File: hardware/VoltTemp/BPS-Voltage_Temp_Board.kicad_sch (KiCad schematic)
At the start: 10 parts, among them J2 PeripheralCAN, J3 PeripheralCAN, J5 Logic_Analyzer, U5 PeripheralSOM

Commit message: schematic mostly done
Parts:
- removed J3: PeripheralCAN, UTSVT_Connectors:Molex_Nano-Fit_105309-xx04_1x04_P2.50mm_Vertical, symbol utsvt_connectors:PeripheralCANConnector
- removed U5: PeripheralSOM, UTSVT_Special:PeripheralSOM, symbol utsvt-misc:PeripheralSOM
- added J10: 53307-2471, UTSVT_Connectors:533072471, symbol utsvt_connectors:PeripheralSOMConnector
- added J12, J13: Conn_01x04, VoltTemp:1053132104, symbol Connector_Generic:Conn_01x04
- added R29: 0Ω, Resistor_SMD:R_0603_1608Metric_Pad0.98x0.95mm_HandSolder, symbol Device:R
- J2: now not fitted; now left out of the parts list
- J5: footprint CONN_SFH11-xxxC-D05-ST-XX_SUL -> UTSVT_Connectors:CONN_SFH11-xxxC-D05-ST-XX_SUL
- LOGO1: footprint UTSVT_Logos:Hallock_Image_Tiny -> UTSVT_Logos:Hallock_Image_Small
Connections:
- net +24V: now also J10.24 (+24V_In), J12.1 (Pin_1), J13.1 (Pin_1); no longer J2.1 (24V)
- net +3.3V: now also J10.2 (+3.3v), R29.2
- net GND: now also J10.1 (GND), J10.3 (GND), J10.5 (GND), J12.4 (Pin_4), J13.4 (Pin_4); no longer J2.2 (GND)
- net GNDA: now also J10.10 (GNDA)
- net I-CAN_H: now also J10.22 (CAN_H), J12.2 (Pin_2), J13.2 (Pin_2); no longer J2.3 (CAN_H)
- net I-CAN_L: now also J10.20 (CAN_L), J12.3 (Pin_3), J13.3 (Pin_3); no longer J2.4 (CAN_L)
- net I2C_SCL: now also J10.6 (I2C1_SCL)
- net I2C_SDA: now also J10.4 (I2C1_SDA)
- net bmsAlert: now also J10.12 (SPI2_NSS)
- net bmsEn: now also J10.19 (SPI1_NSS)
- net LedDin: now reaches J5.5 (CH4)
- net LedDin: now also J10.18 (SPI2_SCK)
- net PB3: now reaches J5.6 (CH5)
- net PB3: now also J10.23 (SPI1_SCK)
- new net Temperature0: J10.9 (ADC1_IN7)
- new net Temperature1: J10.11 (ADC1_IN9)
- new net Temperature2: J10.13 (ADC1_IN10)
- new net Temperature3: J10.15 (ADC1_IN11)
- new net VDDA: J10.8 (VDDA), R29.1
- no-connect marks 14 -> 7
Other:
- added sheet FaultIndicators (FaultIndicators.kicad_sch)
- note added: "PeripheralCAN Connector For pin number reference"
- note added: "Schematic Todo: - Proper CubeMX pinout [X] - Add extra GPIO pins to logic analyzer [] - Assign footprints and P/N [X] - Assign LSC P/N [] - Temperature op amp values - Add debouncing to bms boot button [] - Fix i2c bus[] - LTSpice screenshots for thermistor [] - Derate PTC fuses [] - Add EL3H7 to dl [X] - Make sure optos are fine when regout is 2.5V [X] - Molex Connector pn [X] - Fix all the data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"

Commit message: layout
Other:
- note added: "Schematic Todo: - Proper CubeMX pinout [X] - Add extra GPIO pins to logic analyzer [] - Assign footprints and P/N [X] - Assign LSC P/N [] - Temperature op amp values [] - Add debouncing to bms boot button [] - Fix i2c bus[] - LTSpice screenshots for thermistor [] - Derate PTC fuses [] - Add EL3H7 to dl [X] - Make sure optos are fine when regout is 2.5V [X] - Molex Connector pn [X] - Fix all the d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"
- note removed: "Schematic Todo: - Proper CubeMX pinout [X] - Add extra GPIO pins to logic analyzer [] - Assign footprints and P/N [X] - Assign LSC P/N [] - Temperature op amp values - Add debouncing to bms boot button [] - Fix i2c bus[] - LTSpice screenshots for thermistor [] - Derate PTC fuses [] - Add EL3H7 to dl [X] - Make sure optos are fine when regout is 2.5V [X] - Molex Connector pn [X] - Fix all the data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"
- moved on the sheet: J2
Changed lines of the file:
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@@
 		(comment 4 "Board for measuring voltage and temperature of the battery modules.")
 	)
+	(bus_alias "I2C"
+		(members "I2C_SDA" "I2C_SCL")
+	)
 	(rectangle
 		(start 157.48 67.945)
@@
 		)
 	)
-	(text "Schematic Todo:\n- Proper CubeMX pinout [X]\n- Add extra GPIO pins to logic analyzer []\n- Assign footprints and P/N [X]\n- Assign LSC P/N []\n- Temperature op amp values\n- Add debouncing to bms boot button []\n- Fix i2c bus[]\n- LTSpice screenshots for thermistor []\n- Derate PTC fuses []\n- Add EL3H7 to dl [X]\n- Make sure optos are fine when regout is 2.5V [X]\n- Molex Connector pn [X]\n- Fix all the datasheet as embed symbols [X]\n- Add bypass caps to i2c isolator [X]\n- Change CAN and power connector [X]\n- Fix PB16 (overlapping with PP IMON []"
+	(text "Schematic Todo:\n- Proper CubeMX pinout [X]\n- Add extra GPIO pins to logic analyzer []\n- Assign footprints and P/N [X]\n- Assign LSC P/N []\n- Temperature op amp values []\n- Add debouncing to bms boot button []\n- Fix i2c bus[]\n- LTSpice screenshots for thermistor []\n- Derate PTC fuses []\n- Add EL3H7 to dl [X]\n- Make sure optos are fine when regout is 2.5V [X]\n- Molex Connector pn [X]\n- Fix all the datasheet as embed symbols [X]\n- Add bypass caps to i2c isolator [X]\n- Change CAN and power connector [X]\n- Fix PB16 (overlapping with PP IMON []"
 		(exclude_from_sim no)
 		(at 94.488 167.894 0)
@@
 	(text "PeripheralCAN Connector\nFor pin number reference"
 		(exclude_from_sim no)
-		(at 164.592 43.18 0)
+		(at 164.338 41.656 0)
 		(effects
 			(font
@@
 	(wire
 		(pts
-			(xy 222.25 115.57) (xy 222.25 116.84)
-		)
-		(stroke
-			(width 0)
-			(type default)
-		)
-	)
-	(wire
-		(pts
 			(xy 190.5 35.56) (xy 191.77 35.56)
 		)
@@
 			"rq6p7tKZVhPk8qVwiDi6OtuUFEs+tRON4MrtlEqKyxzhbmH55dR3qR2pF1NjnqVX/+s0jXbd2u79"
 			"LanTqR8XULry74dSg9ntR/9O19Jhb9O61z7+uMsTT6ZeSZ05mDq3cCW1vyg4soEQ6R/yLmIm18Tb"
-			"GxuVOKNKo7+z3Mi4qZE6DZJBIg=="
+			"GxuVOKNKo7+z3Mi4qZE6DZJBIgAkAADlGAAADwAAAOUYAAAPAAAA/////wAkAAD0GAAADwAAAPQY"
+			"AAAPAAAA/////wAkAAADGQAADwAAAAMZAAAPAAAA/////wAkAAASGQAADgAAABIZAAAOAAAA////"
+			"/wAkAAAgGQAABAAAACAZAAAEAAAA/////wAkAAAkGQAACQAAACQZAAAJAAAA/////wAkAAAtGQAA"
+			"BAAAAC0ZAAAEAAAA/////wAkAAAxGQAABAAAADEZAAAEAAAA/////wAkAAA1GQAABgAAADUZAAAG"
+			"AAAA/////wAkAAA7GQAABAAAADsZAAAEAAAA/////wAkAAA/GQAABAAAAD8ZAAAEAAAA/////wAk"
+			"AABDGQAACAAAAEMZAAAIAAAA/////wAkAABLGQAACAAAAEsZAAAIAAAA/////wAkAABTGQAABgAA"
+			"AFMZAAAGAAAA/////wAkAABZGQAABgAAAFkZAAAGAAAA/////wAkAABfGQAABwAAAF8ZAAAHAAAA"
+			"/////wAkAABmGQAABwAAAGYZAAAHAAAA/////wAkAABtGQAACAAAAG0ZAAAIAAAA/////wAkAAB1"
+			"GQAACAAAAHUZAAAIAAAA/////wAkAAB9GQAADAAAAH0ZAAAMAAAA/////wAkAACJGQAAEgAAAIkZ"
+			"AAASAAAA/////wAkAACbGQAAEAAAAJsZAAAQAAAA/////wAkAACrGQAAEQAAAKsZAAARAAAA////"
+			"/wAkAAC8GQAAEAAAALwZAAAQAAAA/////wAkAADMGQAAEQAAAMwZAAARAAAA/////wAkAADdGQAA"
+			"FAAAAN0ZAAAUAAAA/////wAkAADxGQAAEwAAAPEZAAATAAAA/////wAkAAAEGgAAEwAAAAQaAAAT"
+			"AAAA/////wAkAAAXGgAAEwAAABcaAAATAAAA/////wAkAAAqGgAAEwAAACoaAAATAAAA/////wgk"
+			"AAA9GgAAFAAAAD0aAAAUAAAA/////wAkAABRGgAAEwAAAFEaAAATAAAA/////wgkAABkGgAAEwAA"
+			"AGQaAAATAAAA/////wAkAAB3GgAADQAAAHcaAAANAAAA/////wAkAACEGgAAEQAAAIQaAAARAAAA"
+			"/////wgkAACVGgAAFAAAAJUaAAAUAAAA/////wAkAACpGgAADwAAAKkaAAAPAAAA/////wAkAAC4"
+			"GgAAFAAAALgaAAAUAAAA/////wAkAADMGgAAEgAAAMwaAAASAAAA/////wAkAADeGgAAEAAAAN4a"
+			"AAAQAAAA/////wAkAADuGgAAFAAAAO4aAAAUAAAA/////wAkAAACGwAAFQAAAAIbAAAVAAAA////"
+			"/wAkAAAXGwAAFAAAABcbAAAUAA=="
 		)
 	)
@@
 	(symbol
 		(lib_id "power:+3.3V")
-		(at 222.25 115.57 0)
+		(at 222.25 116.84 0)
 		(unit 1)
 		(exclude_from_sim no)
@@
 		(fields_autoplaced yes)
 		(property "Reference" "#PWR080"
-			(at 222.25 119.38 0)
+			(at 222.25 120.65 0)
 			(effects
 				(font
@@
 		)
 		(property "Value" "+3.3V"
-			(at 222.25 110.49 0)
+			(at 222.25 111.76 0)
 			(effects
 				(font
@@
 		)
 		(property "Footprint" ""
-			(at 222.25 115.57 0)
+			(at 222.25 116.84 0)
 			(effects
 				(font
@@
 		)
 		(property "Datasheet" ""
-			(at 222.25 115.57 0)
+			(at 222.25 116.84 0)
 			(effects
 				(font
@@
 		)
 		(property "Description" "Power symbol creates a global label with name \"+3.3V\""
-			(at 222.25 115.57 0)
+			(at 222.25 116.84 0)
 			(effects
 				(font
@@
 	(symbol
 		(lib_id "utsvt_connectors:PeripheralCANConnector")
-		(at 160.02 33.02 0)
+		(at 160.02 31.75 0)
 		(unit 1)
 		(exclude_from_sim yes)
@@
 		(fields_autoplaced yes)
 		(property "Reference" "J2"
-			(at 160.655 22.86 0)
+			(at 160.655 21.59 0)
 			(effects
 				(font
@@
 		)
 		(property "Value" "PeripheralCAN"
-			(at 160.655 25.4 0)
+			(at 160.655 24.13 0)
 			(effects
 				(font
@@
 		)
 		(property "Footprint" "UTSVT_Connectors:Molex_Nano-Fit_105309-xx04_1x04_P2.50mm_Vertical"
-			(at 160.02 41.91 0)
+			(at 160.02 40.64 0)
 			(effects
 				(font
@@
 		)
 		(property "Datasheet" "https://www.mouser.com/ProductDetail/Molex/105309-1204?qs=PqFvFmEiOr6mDAWV2BJKbg%3D%3D&srsltid=AfmBOopk7YsqdMLo2_DAHKaHKt3Hg126ooPXYWv5Q2Pfx6rW7DaYZCT2"
-			(at 165.1 25.4 0)
+			(at 165.1 24.13 0)
 			(effects
 				(font
@@
 		)
 		(property "Description" "Connection to the car's Peripheral CAN bus."
-			(at 160.02 33.02 0)
+			(at 160.02 31.75 0)
 			(effects
 				(font
@@
 		)
 		(property "P/N" "105309-1204 "
-			(at 160.02 33.02 0)
+			(at 160.02 31.75 0)
 			(effects
 				(font

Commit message: layout2 electric boogaloo
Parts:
- added R14, R15: 10kΩ, Resistor_SMD:R_0603_1608Metric_Pad0.98x0.95mm_HandSolder, symbol Device:R
- J10: footprint UTSVT_Connectors:533072471 -> UTSVT_Connectors:PeripheralSOM
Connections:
- net +3.3V: now also R14.2, R15.2
- net I2C_SCL: now also J5.8 (CH7), R15.1; no longer J5.2 (CH1)
- net I2C_SDA: now also J5.7 (CH6), R14.1; no longer J5.1 (CH0)
- no-connect marks 7 -> 12
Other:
- note added: "Schematic Todo: - Proper CubeMX pinout [X] - Add extra GPIO pins to logic analyzer [] - Assign footprints and P/N [X] - Assign LSC P/N [] - Temperature op amp values [] - Fix i2c bus[X] - LTSpice screenshots for thermistor [] - Derate PTC fuses [] - Add EL3H7 to dl [X] - Make sure optos are fine when regout is 2.5V [X] - Molex Connector pn [X] - Fix all the datasheet as embed symbols [X] - Add by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"
- note removed: "Schematic Todo: - Proper CubeMX pinout [X] - Add extra GPIO pins to logic analyzer [] - Assign footprints and P/N [X] - Assign LSC P/N [] - Temperature op amp values [] - Add debouncing to bms boot button [] - Fix i2c bus[] - LTSpice screenshots for thermistor [] - Derate PTC fuses [] - Add EL3H7 to dl [X] - Make sure optos are fine when regout is 2.5V [X] - Molex Connector pn [X] - Fix all the d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"
- moved on the sheet: R29

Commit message: most layout done
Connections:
- net Temperature0: now also J10.7 (OPAMP1_VINP); no longer J10.9 (ADC1_IN7)
- net Temperature1: now also J10.15 (ADC1_IN11); no longer J10.11 (ADC1_IN9)
- net Temperature3: now also J10.11 (ADC1_IN9); no longer J10.15 (ADC1_IN11)
- net Temperature4: now also J10.9 (ADC1_IN7)
- net PB15: now reaches J5.1 (CH0)
- net PB15: now also J10.16 (SPI2_MOSI)
- net PB14: now reaches J5.2 (CH1)
- net PB14: now also J10.14 (SPI2_MISO)
- no-connect marks 12 -> 10
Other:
- sheet VoltageConn ports: added last_cell; removed none
- sheet VoltageSense ports: added last_cell; removed none
- note added: "Schematic Todo: - Proper CubeMX pinout [X] - Add extra GPIO pins to logic analyzer [] - Assign footprints and P/N [X] - Assign LSC P/N [] - Temperature op amp values [X] - Fix i2c bus[X] - LTSpice screenshots for thermistor [X] - Derate PTC fuses [] - Add EL3H7 to dl [X] - Make sure optos are fine when regout is 2.5V [X] - Molex Connector pn [X] - Fix all the datasheet as embed symbols [X] - Add 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"
- note removed: "Schematic Todo: - Proper CubeMX pinout [X] - Add extra GPIO pins to logic analyzer [] - Assign footprints and P/N [X] - Assign LSC P/N [] - Temperature op amp values [] - Fix i2c bus[X] - LTSpice screenshots for thermistor [] - Derate PTC fuses [] - Add EL3H7 to dl [X] - Make sure optos are fine when regout is 2.5V [X] - Molex Connector pn [X] - Fix all the datasheet as embed symbols [X] - Add by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"

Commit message: some ocd stuff
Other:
- note added: "Schematic Todo: - Proper CubeMX pinout [X] - Add extra GPIO pins to logic analyzer [X] - Assign footprints and P/N [X] - Assign LSC P/N [] - Temperature op amp values [X] - Fix i2c bus[X] - LTSpice screenshots for thermistor [X] - Derate PTC fuses [] - Add EL3H7 to dl [X] - Make sure optos are fine when regout is 2.5V [X] - Molex Connector pn [X] - Fix all the datasheet as embed symbols [X] - Add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"
- note removed: "Schematic Todo: - Proper CubeMX pinout [X] - Add extra GPIO pins to logic analyzer [] - Assign footprints and P/N [X] - Assign LSC P/N [] - Temperature op amp values [X] - Fix i2c bus[X] - LTSpice screenshots for thermistor [X] - Derate PTC fuses [] - Add EL3H7 to dl [X] - Make sure optos are fine when regout is 2.5V [X] - Molex Connector pn [X] - Fix all the datasheet as embed symbols [X] - Add 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"
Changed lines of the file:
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@@
 		)
 	)
-	(text "Schematic Todo:\n- Proper CubeMX pinout [X]\n- Add extra GPIO pins to logic analyzer []\n- Assign footprints and P/N [X]\n- Assign LSC P/N []\n- Temperature op amp values [X]\n- Fix i2c bus[X]\n- LTSpice screenshots for thermistor [X]\n- Derate PTC fuses []\n- Add EL3H7 to dl [X]\n- Make sure optos are fine when regout is 2.5V [X]\n- Molex Connector pn [X]\n- Fix all the datasheet as embed symbols [X]\n- Add bypass caps to i2c isolator [X]\n- Change CAN and power connector [X]\n- Fix PB16 (overlapping with PP IMON [X]"
+	(text "Schematic Todo:\n- Proper CubeMX pinout [X]\n- Add extra GPIO pins to logic analyzer [X]\n- Assign footprints and P/N [X]\n- Assign LSC P/N []\n- Temperature op amp values [X]\n- Fix i2c bus[X]\n- LTSpice screenshots for thermistor [X]\n- Derate PTC fuses []\n- Add EL3H7 to dl [X]\n- Make sure optos are fine when regout is 2.5V [X]\n- Molex Connector pn [X]\n- Fix all the datasheet as embed symbols [X]\n- Add bypass caps to i2c isolator [X]\n- Change CAN and power connector [X]\n- Fix PB16 (overlapping with PP IMON [X]"
 		(exclude_from_sim no)
 		(at 94.488 167.894 0)

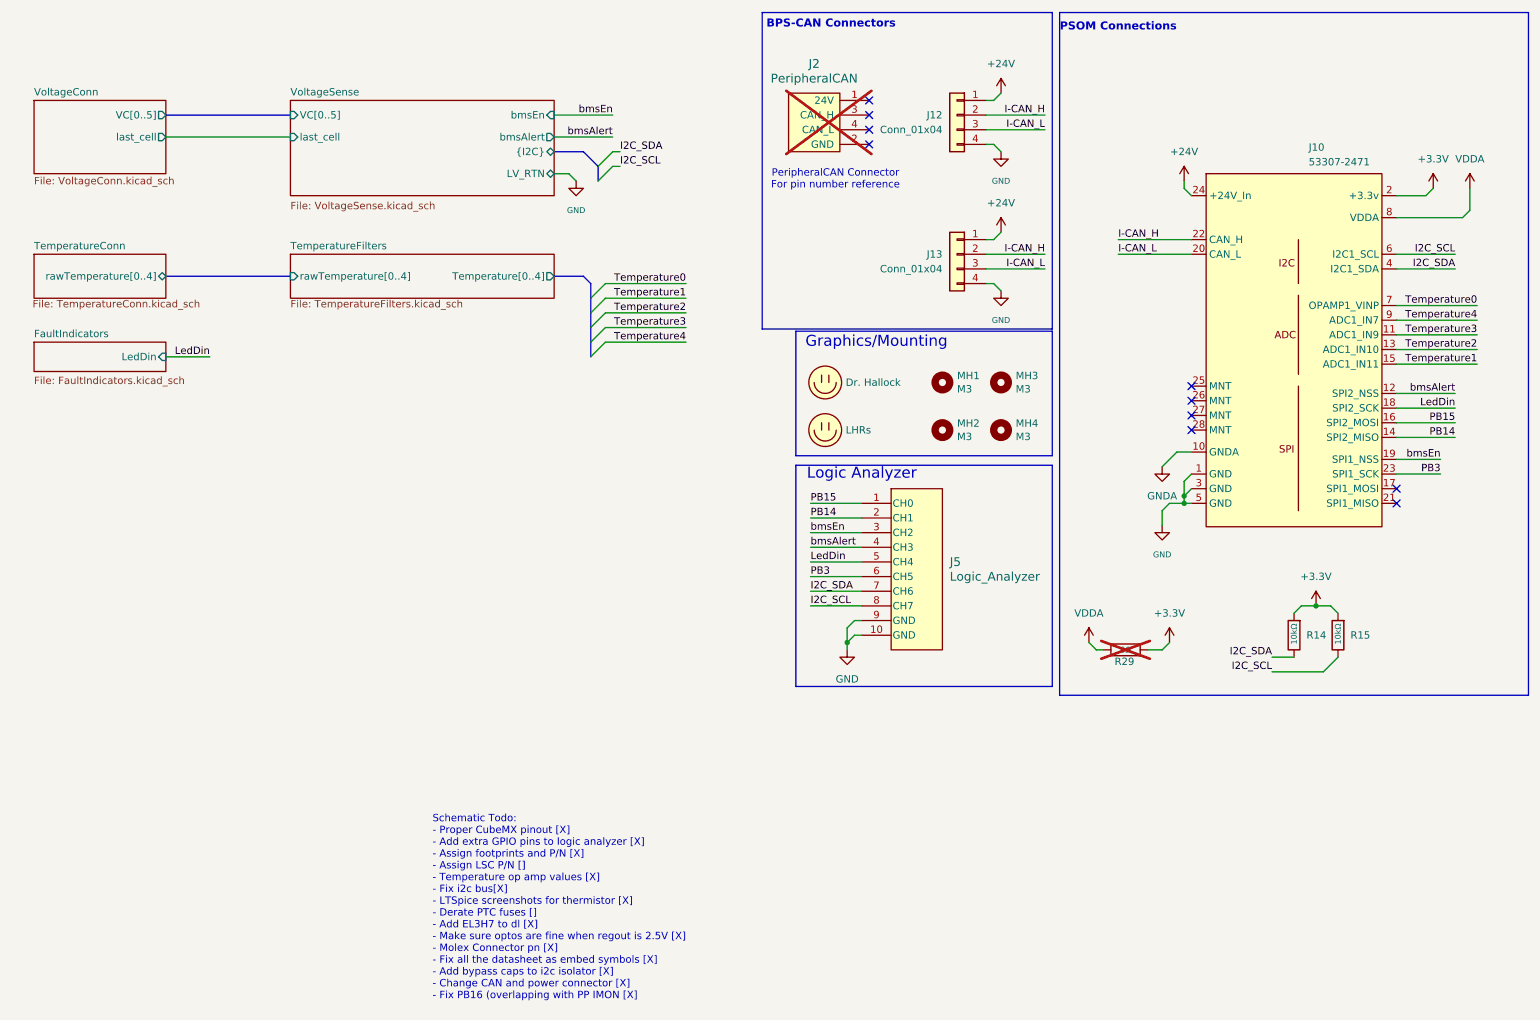
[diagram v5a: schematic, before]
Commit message: add thermistor test board, just need to route volttemp testpoints
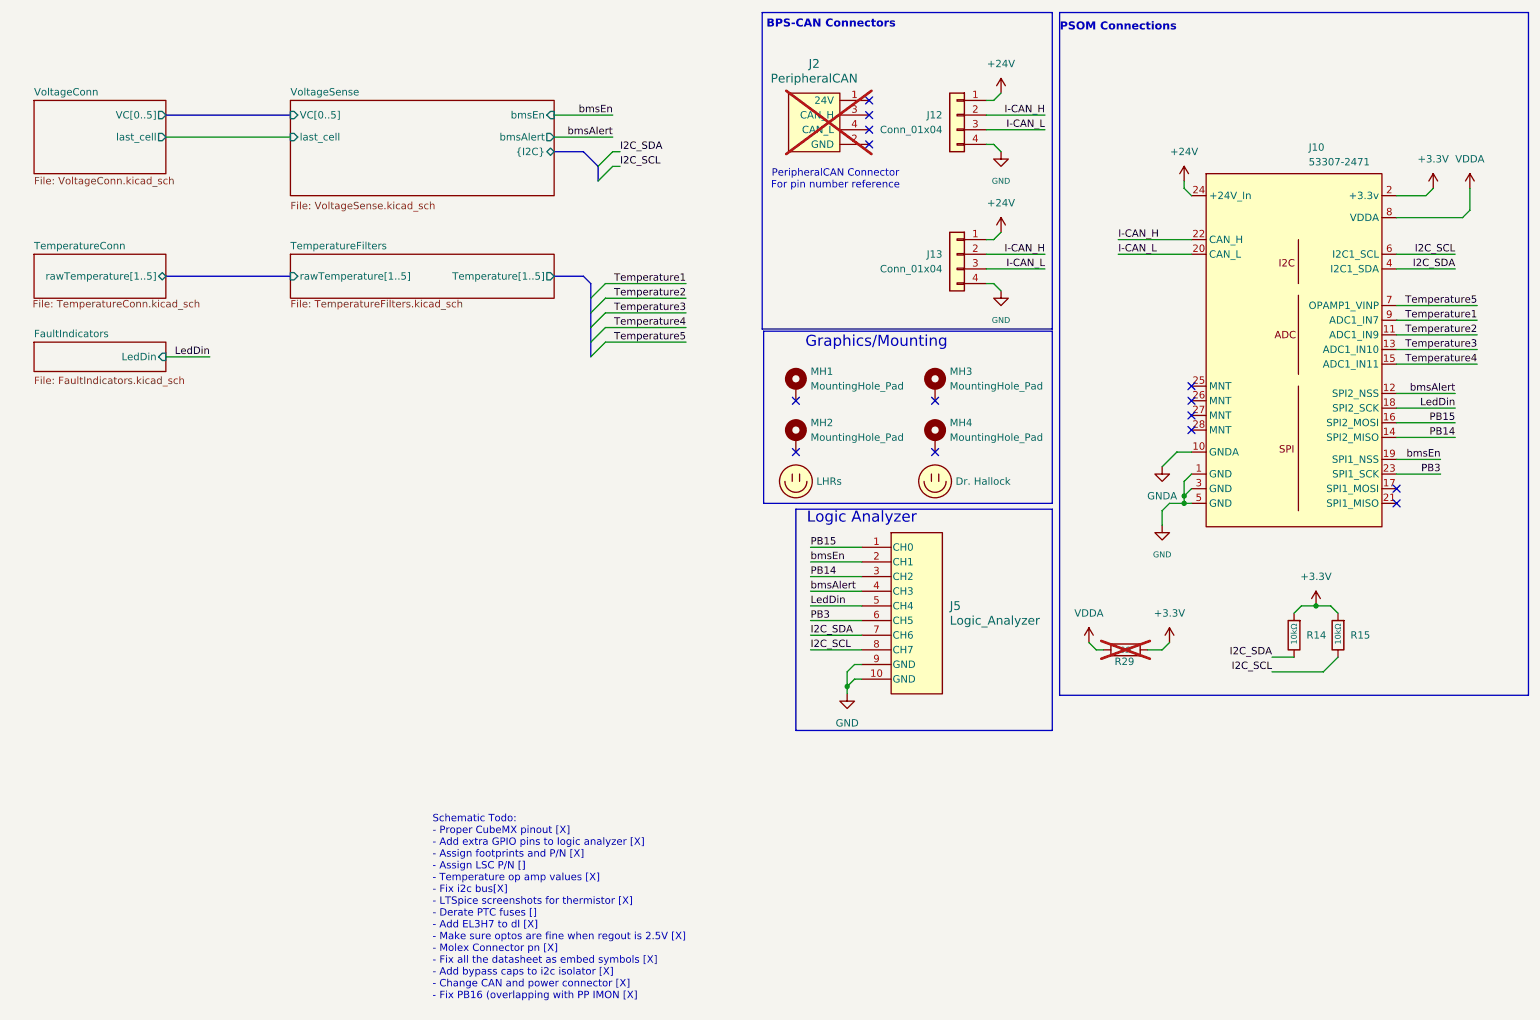
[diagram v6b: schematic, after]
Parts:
- removed MH1, MH2, MH3, MH4: M3, MountingHole:MountingHole_3.2mm_M3_Pad_TopBottom, symbol Mechanical:MountingHole
- added MH1, MH2, MH3, MH4: MountingHole_Pad, MountingHole:MountingHole_3.2mm_M3_Pad_TopBottom, symbol Mechanical:MountingHole_Pad
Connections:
- net PB14: now also J5.3 (CH2); no longer J5.2 (CH1)
- net Temperature1: now also J10.9 (ADC1_IN7); no longer J10.15 (ADC1_IN11)
- net Temperature2: now also J10.11 (ADC1_IN9); no longer J10.13 (ADC1_IN10)
- net Temperature3: now also J10.13 (ADC1_IN10); no longer J10.11 (ADC1_IN9)
- net Temperature4: now also J10.15 (ADC1_IN11); no longer J10.9 (ADC1_IN7)
- net bmsEn: now also J5.2 (CH1); no longer J5.3 (CH2)
- net Temperature0 renamed Temperature5
- no-connect marks 10 -> 14
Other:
- sheet TemperatureConn ports: added rawTemperature[1..5]; removed rawTemperature[0..4]
- sheet TemperatureFilters ports: added Temperature[1..5], rawTemperature[1..5]; removed Temperature[0..4], rawTemperature[0..4]
- sheet VoltageSense ports: added none; removed LV_RTN
- moved on the sheet: J5
